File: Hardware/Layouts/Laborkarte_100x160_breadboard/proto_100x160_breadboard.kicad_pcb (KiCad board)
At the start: 2 copper layers, 100 x 160 mm, 1946 parts

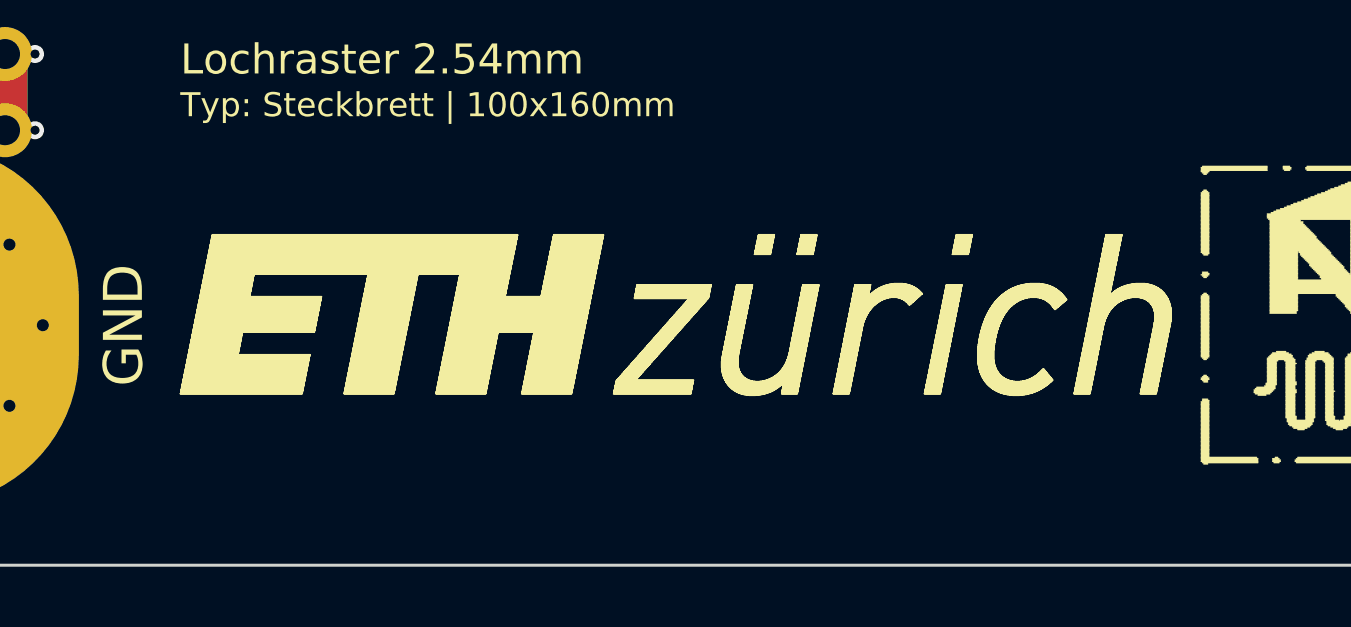
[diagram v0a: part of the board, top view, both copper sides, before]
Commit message: Fix ETH logo visibility, add violet PCB background, show F+B sides
- Downscale high-res logo images before rasterizing so line width
  stays visible (ETH logo was 0.005mm, now 0.02mm)
- Preview images now show front and back side by side
- Board background changed to JLCPCB violet
- PDF updated with filled copper zones and fixed silkscreen parsing
- All Gerbers and ZIPs regenerated
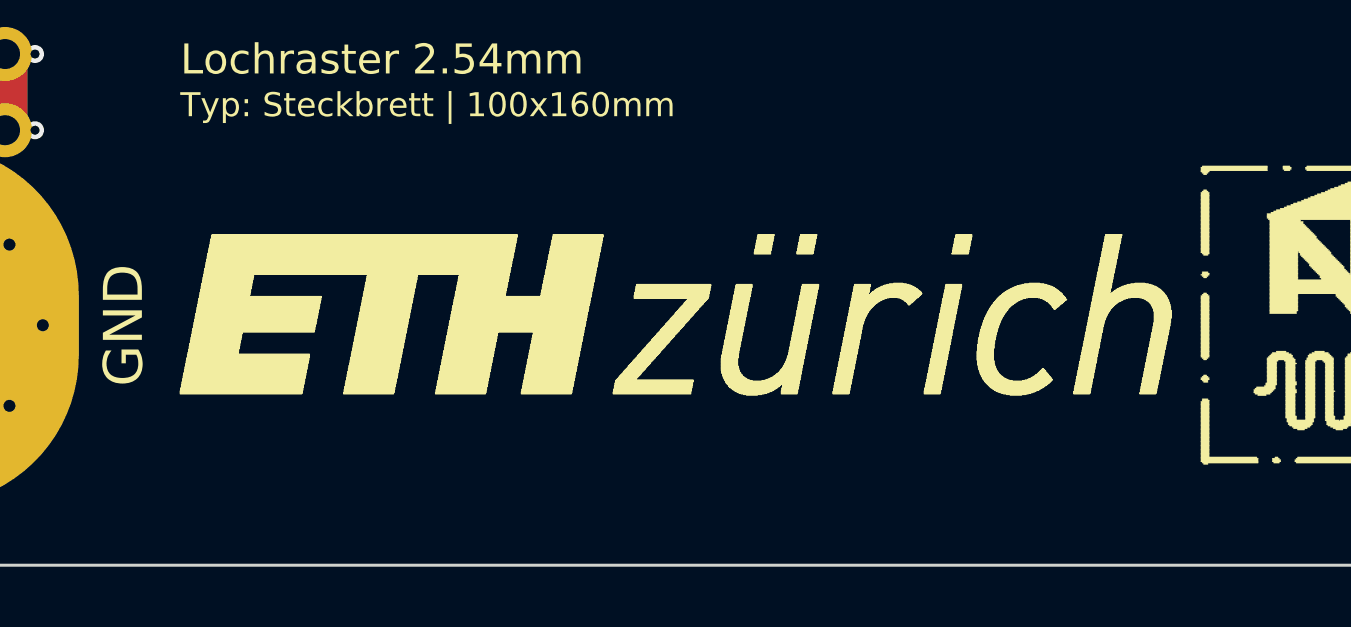
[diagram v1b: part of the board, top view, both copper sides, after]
